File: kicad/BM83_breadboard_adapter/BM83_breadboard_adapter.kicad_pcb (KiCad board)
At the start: 2 copper layers, 38.1 x 99.1 mm, 65 parts, among them J1 PJ-320B, J2 PJ-320B, J3 USB_B_Micro, J4 Conn_01x25_Female, J5 Conn_01x25_Female, J6 PJ-320B, SW1 VOL-, SW2 VOL+, SW3 PREV, SW4 NEXT, SW6 PLAY, SW7 SELECT, SW8 MFB, SW9 RESET, U1 BM83, U2 PJ-3027F

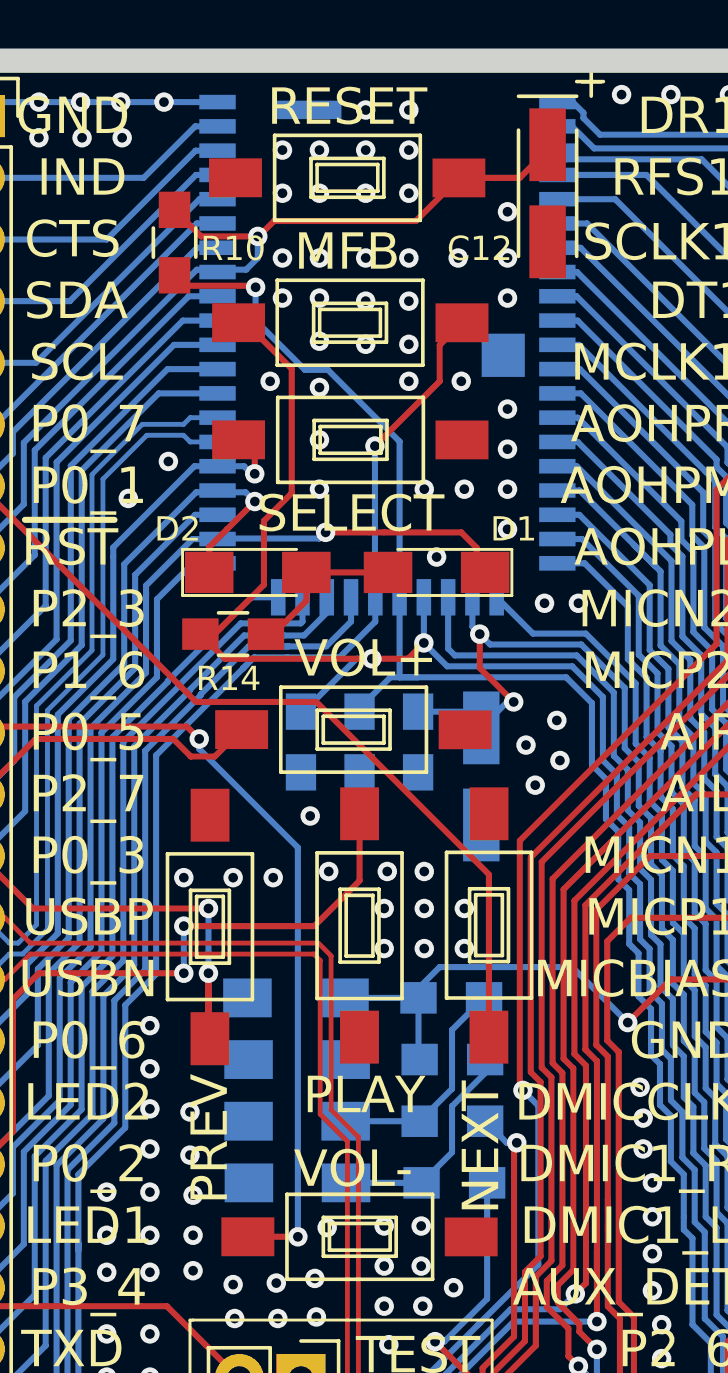
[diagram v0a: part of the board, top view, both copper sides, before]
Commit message: update BM83 footprint on board!
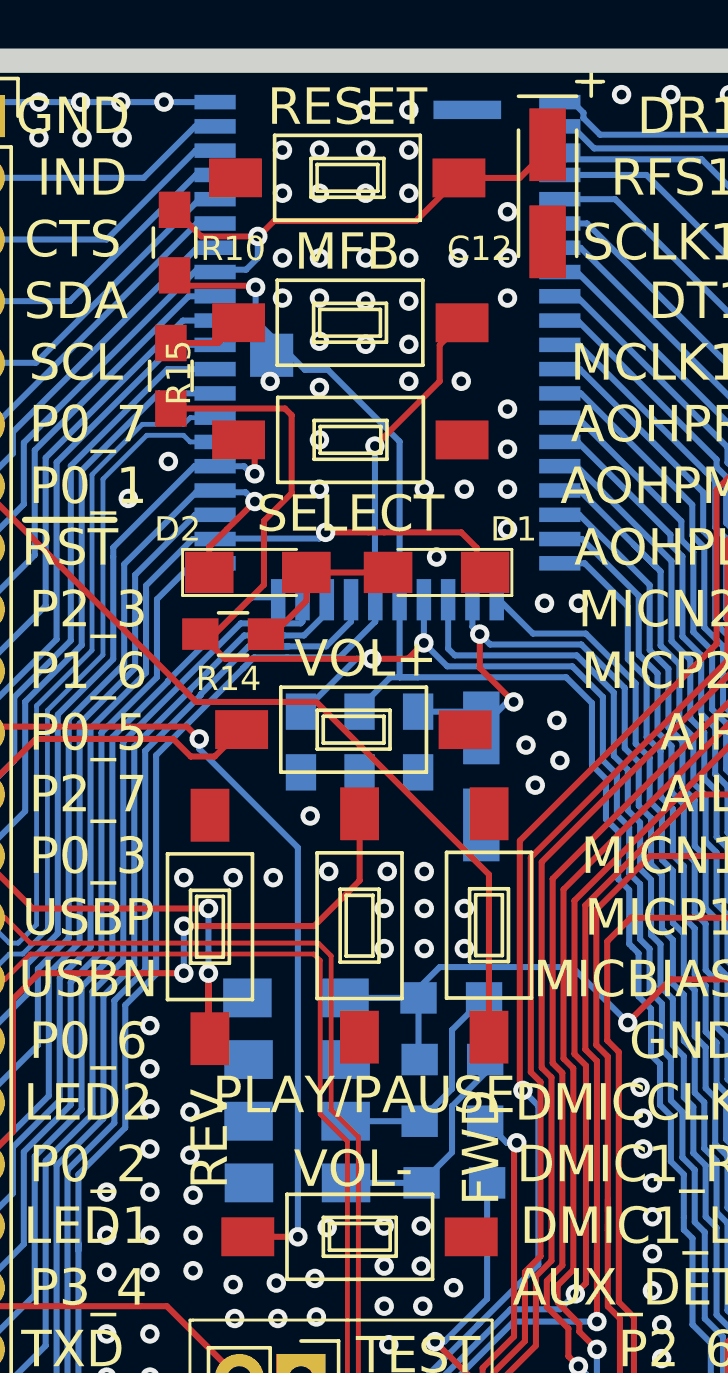
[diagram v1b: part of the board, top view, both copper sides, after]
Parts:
- added R15: 1k, Resistors_SMD.pretty:R_0805_HandSoldering, F.Cu at (505.7, -438.9)
- SW3: value PREV -> REV
- SW4: value NEXT -> FWD
- SW6: value PLAY -> PLAY/PAUSE
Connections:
- SW8 pad 2: /SYS_PWR -> Net-(R15-Pad1)
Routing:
- net Net-(R15-Pad1): track 0.00 -> 3.43 mm

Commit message: fixies
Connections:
- net /~RST renamed /~{RST}
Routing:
- net /VDD_IO: track 74.1 -> 75.0 mm
- net GND: vias 316 -> 313
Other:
- net class Default removed
- board text added: "~{RST}"
- board text removed: "~RST"

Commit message: update
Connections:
- J3 pad 4: (no net) -> unconnected-(J3-Pad4)
